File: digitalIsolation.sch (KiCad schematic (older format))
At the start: 9 parts, among them U14 74AHC1G14, U15 Si8651

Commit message: Extended board
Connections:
- net SDO: now also RP1.5 (R4); no longer R25.1
- net ~LDAC: now also R25.1; no longer RP1.5 (R4)
- net at U15.11 (B5): now also RP1.4 (P4); no longer R25.2
- net at U15.12 (B4): now also R25.2; no longer RP1.4 (P4)
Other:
- moved on the sheet: R25, RP1
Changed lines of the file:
@@
 Comment4 ""
 $EndDescr
-Text HLabel 8700 2250 2    60   Output ~ 0
+Text HLabel 8700 2200 2    60   Output ~ 0
 ~SS
-Text HLabel 8700 2350 2    60   Output ~ 0
+Text HLabel 8700 2300 2    60   Output ~ 0
 SCLK
-Text HLabel 8700 2450 2    60   Output ~ 0
+Text HLabel 8700 2400 2    60   Output ~ 0
 SDI
-Text HLabel 8700 2800 2    60   Input ~ 0
+Text HLabel 8700 2500 2    60   Input ~ 0
 SDO
-Text HLabel 8700 2550 2    60   Output ~ 0
+Text HLabel 8700 2700 2    60   Output ~ 0
 ~LDAC
 $Comp
@@
 $EndComp
 Wire Wire Line
-	8000 2350 7700 2350
-Wire Wire Line
-	7700 2800 8050 2800
-Wire Wire Line
 	7700 2950 7800 2950
 Wire Wire Line
@@
 	6400 3500 6300 3500
 Wire Wire Line
-	6300 3500 6300 3800
+	6300 3800 6300 3500
 $Comp
 L C C73
@@
 	4400 3650 4400 3800
 Wire Wire Line
-	6300 3800 3600 3800
+	3600 3800 6300 3800
 Connection ~ 5200 3800
 Connection ~ 6000 3800
@@
 L R R25
 U 1 1 56E0FC32
-P 8200 2800
-F 0 "R25" V 8280 2800 50  0000 C CNN
-F 1 "150" V 8200 2800 50  0000 C CNN
-F 2 "Resistors_SMD:R_0805" V 8130 2800 50  0001 C CNN
-F 3 "" H 8200 2800 50  0000 C CNN
-F 4 "MCWR08X1500FTL" H 8200 2800 60  0001 C CNN "Part Number"
-F 5 "Multicomp" H 8200 2800 60  0001 C CNN "Manufacturer"
-F 6 "0805" H 8200 2800 60  0001 C CNN "Package"
-F 7 "Farnell" H 8200 2800 60  0001 C CNN "Supplier"
-F 8 "2447574" H 8200 2800 60  0001 C CNN "Order Code"
-F 9 "Mouser" H 8200 2800 60  0001 C CNN "Alt. Supplier"
-F 10 "71-TNPW0805150RFEEA" H 8200 2800 60  0001 C CNN "Alt. Order Code"
-F 11 "150Ω/1% 0805 resistor" H 8200 2800 60  0001 C CNN "Note"
-	1    8200 2800
+P 8200 2700
+F 0 "R25" V 8280 2700 50  0000 C CNN
+F 1 "150" V 8200 2700 50  0000 C CNN
+F 2 "Resistors_SMD:R_0805" V 8130 2700 50  0001 C CNN
+F 3 "" H 8200 2700 50  0000 C CNN
+F 4 "MCWR08X1500FTL" H 8200 2700 60  0001 C CNN "Part Number"
+F 5 "Multicomp" H 8200 2700 60  0001 C CNN "Manufacturer"
+F 6 "0805" H 8200 2700 60  0001 C CNN "Package"
+F 7 "Farnell" H 8200 2700 60  0001 C CNN "Supplier"
+F 8 "2447574" H 8200 2700 60  0001 C CNN "Order Code"
+F 9 "Mouser" H 8200 2700 60  0001 C CNN "Alt. Supplier"
+F 10 "71-TNPW0805150RFEEA" H 8200 2700 60  0001 C CNN "Alt. Order Code"
+F 11 "150Ω/1% 0805 resistor" H 8200 2700 60  0001 C CNN "Note"
+	1    8200 2700
 	0    1    1    0
 $EndComp
 Wire Wire Line
-	8400 2250 8700 2250
-Wire Wire Line
-	8400 2350 8700 2350
-Wire Wire Line
-	8400 2450 8700 2450
-Wire Wire Line
-	8400 2550 8700 2550
-Wire Wire Line
-	8350 2800 8700 2800
+	8400 2200 8700 2200
+Wire Wire Line
+	8400 2300 8700 2300
+Wire Wire Line
+	8400 2400 8700 2400
+Wire Wire Line
+	8350 2700 8700 2700
+Wire Wire Line
+	8400 2500 8700 2500
 $Comp
 L R_PACK4 RP1
 U 1 1 56E10B8D
-P 8200 2600
-F 0 "RP1" H 8200 3050 50  0000 C CNN
-F 1 "4x150" H 8200 2550 50  0000 C CNN
-F 2 "Resistors_SMD:R_Array_Convex_4x0603" H 8200 2600 50  0001 C CNN
-F 3 "" H 8200 2600 50  0000 C CNN
-F 4 "YC164-JR-07150RL" H 8200 2600 60  0001 C CNN "Part Number"
-F 5 "Yageo" H 8200 2600 60  0001 C CNN "Manufacturer"
-F 6 "4×0603" H 8200 2600 60  0001 C CNN "Package"
-F 7 "Farnell" H 8200 2600 60  0001 C CNN "Supplier"
-F 8 "9234462" H 8200 2600 60  0001 C CNN "Order Code"
-F 9 "Mouser" H 8200 2600 60  0001 C CNN "Alt. Supplier"
-F 10 "603-YC164-JR-07150RL" H 8200 2600 60  0001 C CNN "Alt. Order Code"
-F 11 "4×150Ω/5% 0603 resistor array" H 8200 2600 60  0001 C CNN "Note"
-	1    8200 2600
-	1    0    0    -1
-$EndComp
-Wire Wire Line
-	7700 2200 7900 2200
-Wire Wire Line
-	7900 2200 7900 2250
-Wire Wire Line
-	7900 2250 8000 2250
-Wire Wire Line
-	8000 2450 7900 2450
-Wire Wire Line
-	7900 2450 7900 2500
-Wire Wire Line
-	7900 2500 7700 2500
-Wire Wire Line
-	7700 2650 7900 2650
-Wire Wire Line
-	7900 2650 7900 2550
-Wire Wire Line
-	7900 2550 8000 2550
+P 8200 2550
+F 0 "RP1" H 8200 3000 50  0000 C CNN
+F 1 "4x150" H 8200 2500 50  0000 C CNN
+F 2 "Resistors_SMD:R_Array_Convex_4x0603" H 8200 2550 50  0001 C CNN
+F 3 "" H 8200 2550 50  0000 C CNN
+F 4 "YC164-JR-07150RL" H 8200 2550 60  0001 C CNN "Part Number"
+F 5 "Yageo" H 8200 2550 60  0001 C CNN "Manufacturer"
+F 6 "4×0603" H 8200 2550 60  0001 C CNN "Package"
+F 7 "Farnell" H 8200 2550 60  0001 C CNN "Supplier"
+F 8 "9234462" H 8200 2550 60  0001 C CNN "Order Code"
+F 9 "Mouser" H 8200 2550 60  0001 C CNN "Alt. Supplier"
+F 10 "603-YC164-JR-07150RL" H 8200 2550 60  0001 C CNN "Alt. Order Code"
+F 11 "4×150Ω/5% 0603 resistor array" H 8200 2550 60  0001 C CNN "Note"
+	1    8200 2550
+	1    0    0    -1
+$EndComp
+Wire Wire Line
+	7700 2200 8000 2200
 $Comp
 L C C76
@@
 	1    0    0    -1
 $EndComp
+Wire Wire Line
+	8000 2300 7800 2300
+Wire Wire Line
+	7800 2300 7800 2350
+Wire Wire Line
+	7800 2350 7700 2350
+Wire Wire Line
+	8000 2400 7850 2400
+Wire Wire Line
+	7850 2400 7850 2500
+Wire Wire Line
+	7850 2500 7700 2500
+Wire Wire Line
+	8000 2500 7900 2500
+Wire Wire Line
+	7900 2500 7900 2800
+Wire Wire Line
+	7900 2800 7700 2800
+Wire Wire Line
+	7700 2650 7800 2650
+Wire Wire Line
+	7800 2650 7800 2700
+Wire Wire Line
+	7800 2700 8050 2700
 $EndSCHEMATC

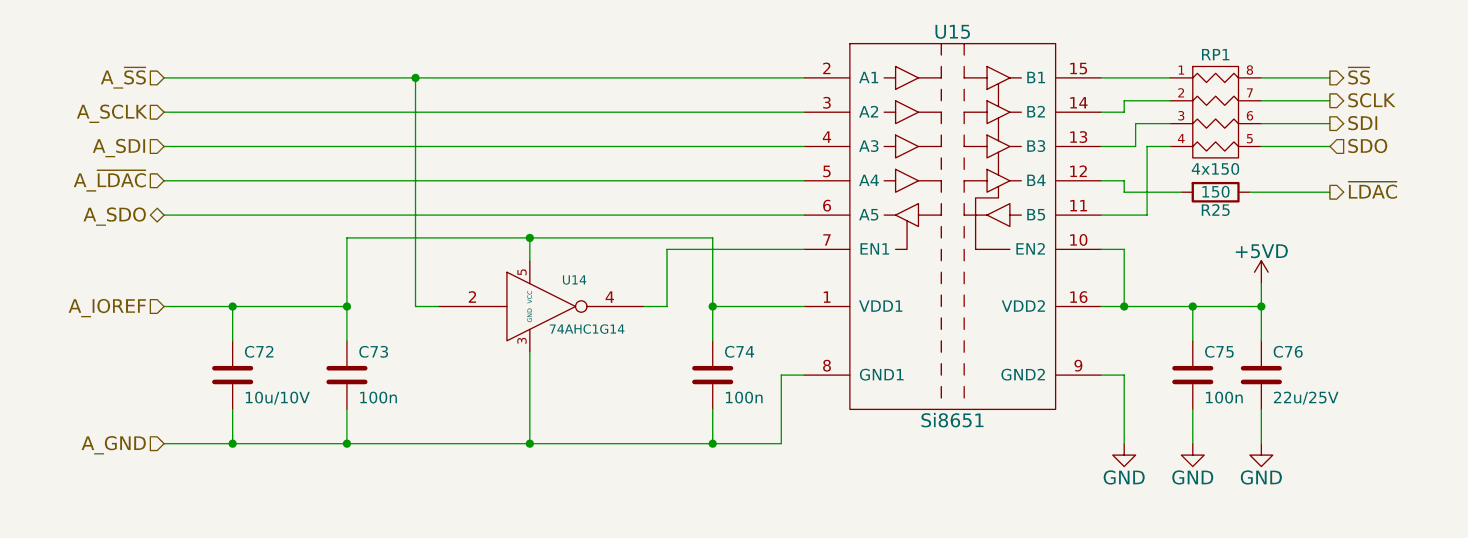
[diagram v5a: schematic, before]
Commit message: Fixed can, 1Ohm resistor descriptions
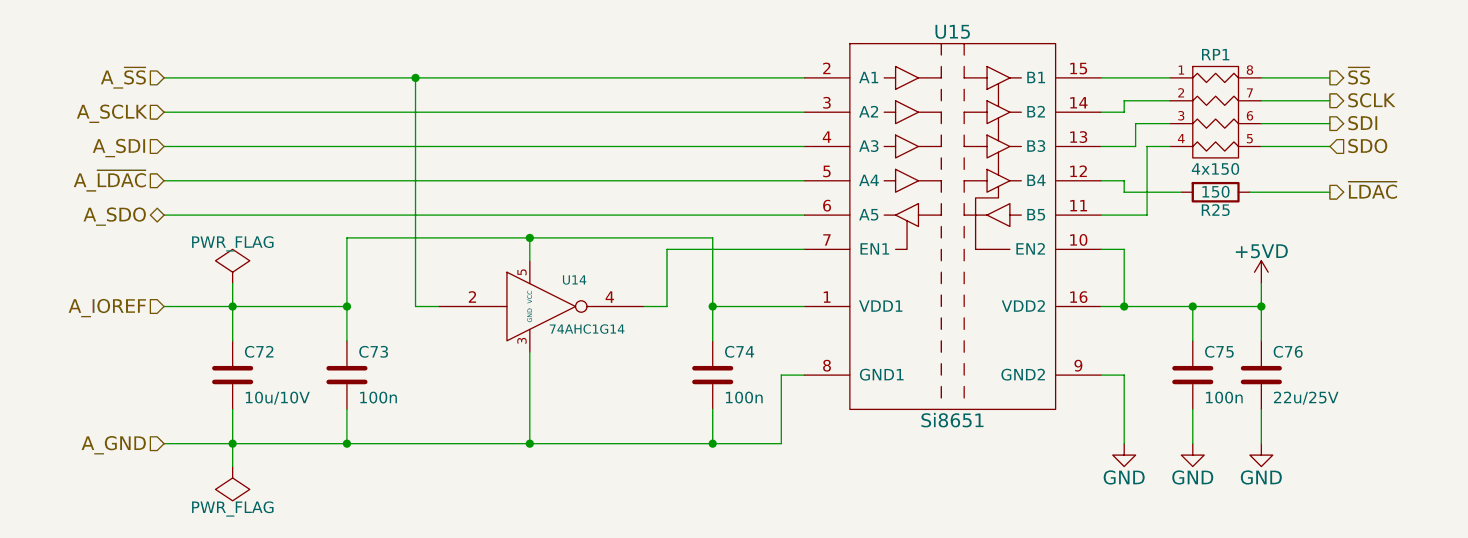
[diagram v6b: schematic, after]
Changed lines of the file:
@@
 	8100 3650 8100 3800
 $Comp
-L GND #PWR082
+L GND #PWR089
 U 1 1 5574AC81
 P 7800 3800
-F 0 "#PWR082" H 7800 3550 60  0001 C CNN
+F 0 "#PWR089" H 7800 3550 60  0001 C CNN
 F 1 "GND" H 7800 3650 60  0000 C CNN
 F 2 "" H 7800 3800 60  0000 C CNN
@@
 $EndComp
 $Comp
-L GND #PWR083
+L GND #PWR090
 U 1 1 5574ACAE
 P 8100 3800
-F 0 "#PWR083" H 8100 3550 60  0001 C CNN
+F 0 "#PWR090" H 8100 3550 60  0001 C CNN
 F 1 "GND" H 8100 3650 60  0000 C CNN
 F 2 "" H 8100 3800 60  0000 C CNN
@@
 	6400 3500 6300 3500
 Wire Wire Line
-	6300 3800 6300 3500
+	6300 3500 6300 3800
 $Comp
 L C C73
@@
 	4400 3650 4400 3800
 Wire Wire Line
-	3600 3800 6300 3800
+	6300 3800 3600 3800
 Connection ~ 5200 3800
 Connection ~ 6000 3800
@@
 $EndComp
 Wire Wire Line
-	3900 3350 3900 3200
+	3900 3100 3900 3350
 Connection ~ 3900 3200
 Wire Wire Line
-	3900 3650 3900 3800
+	3900 3650 3900 3900
 Connection ~ 3900 3800
 $Comp
@@
 Connection ~ 8400 3200
 $Comp
-L +5VD #PWR084
+L +5VD #PWR091
 U 1 1 5574AC36
 P 8400 3100
-F 0 "#PWR084" H 8400 2950 60  0001 C CNN
+F 0 "#PWR091" H 8400 2950 60  0001 C CNN
 F 1 "+5VD" H 8400 3240 60  0000 C CNN
 F 2 "" H 8400 3100 60  0000 C CNN
@@
 	8400 3650 8400 3800
 $Comp
-L GND #PWR085
+L GND #PWR092
 U 1 1 56E16784
 P 8400 3800
-F 0 "#PWR085" H 8400 3550 60  0001 C CNN
+F 0 "#PWR092" H 8400 3550 60  0001 C CNN
 F 1 "GND" H 8400 3650 60  0000 C CNN
 F 2 "" H 8400 3800 60  0000 C CNN
@@
 Wire Wire Line
 	7800 2700 8050 2700
+$Comp
+L PWR_FLAG #FLG093
+U 1 1 56F3D1DA
+P 3900 3100
+F 0 "#FLG093" H 3900 3195 50  0001 C CNN
+F 1 "PWR_FLAG" H 3900 3280 50  0000 C CNN
+F 2 "" H 3900 3100 50  0000 C CNN
+F 3 "" H 3900 3100 50  0000 C CNN
+	1    3900 3100
+	1    0    0    -1
+$EndComp
+$Comp
+L PWR_FLAG #FLG094
+U 1 1 56F3D24A
+P 3900 3900
+F 0 "#FLG094" H 3900 3995 50  0001 C CNN
+F 1 "PWR_FLAG" H 3900 4080 50  0000 C CNN
+F 2 "" H 3900 3900 50  0000 C CNN
+F 3 "" H 3900 3900 50  0000 C CNN
+	1    3900 3900
+	-1   0    0    1
+$EndComp
 $EndSCHEMATC

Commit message: Finalized PCB for production
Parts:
- C72: Alt. Order Code 81-GRM21BR61A106KE19 -> 603-CC805KKX5R8BB106
- C73, C74, C75: Alt. Order Code 710-885012206095 -> 603-CC603KRX7R9BB104; Manufacturer Multicomp -> Yageo; Note 100n/50V X7R 0603 ceramic capacitor -> 100nF/50V X7R 0603 ceramic capacitor; Order Code 1759122 -> 1362556; Part Number MC0603B104K500CT -> CC0603KRX7R9BB104
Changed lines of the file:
@@
 Wire Wire Line
 	7700 3200 8400 3200
-$Comp
-L C C75
-U 1 1 5574AB6E
-P 8100 3500
-F 0 "C75" H 8150 3600 50  0000 L CNN
-F 1 "100n" H 8150 3400 50  0000 L CNN
-F 2 "Capacitors_SMD:C_0603" H 8138 3350 30  0001 C CNN
-F 3 "" H 8100 3500 60  0000 C CNN
-F 4 "MC0603B104K500CT" H 5300 7000 60  0001 C CNN "Part Number"
-F 5 "Multicomp" H 5300 7000 60  0001 C CNN "Manufacturer"
-F 6 "0603" H 8100 3500 60  0001 C CNN "Package"
-F 7 "Farnell" H 8100 3500 60  0001 C CNN "Supplier"
-F 8 "1759122" H 5300 7000 60  0001 C CNN "Order Code"
-F 9 "Mouser" H 8100 3500 60  0001 C CNN "Alt. Supplier"
-F 10 "710-885012206095" H 8100 3500 60  0001 C CNN "Alt. Order Code"
-F 11 "100n/50V X7R 0603 ceramic capacitor" H 8100 3500 60  0001 C CNN "Note"
-	1    8100 3500
-	1    0    0    -1
-$EndComp
 Wire Wire Line
 	8100 3200 8100 3350
@@
 	8100 3650 8100 3800
 $Comp
-L GND #PWR089
+L GND #PWR85
 U 1 1 5574AC81
 P 7800 3800
-F 0 "#PWR089" H 7800 3550 60  0001 C CNN
+F 0 "#PWR85" H 7800 3550 60  0001 C CNN
 F 1 "GND" H 7800 3650 60  0000 C CNN
 F 2 "" H 7800 3800 60  0000 C CNN
@@
 $EndComp
 $Comp
-L GND #PWR090
+L GND #PWR86
 U 1 1 5574ACAE
 P 8100 3800
-F 0 "#PWR090" H 8100 3550 60  0001 C CNN
+F 0 "#PWR86" H 8100 3550 60  0001 C CNN
 F 1 "GND" H 8100 3650 60  0000 C CNN
 F 2 "" H 8100 3800 60  0000 C CNN
@@
 	1    0    0    -1
 $EndComp
-$Comp
-L C C74
-U 1 1 5574AE37
-P 6000 3500
-F 0 "C74" H 6050 3600 50  0000 L CNN
-F 1 "100n" H 6050 3400 50  0000 L CNN
-F 2 "Capacitors_SMD:C_0603" H 6038 3350 30  0001 C CNN
-F 3 "" H 6000 3500 60  0000 C CNN
-F 4 "MC0603B104K500CT" H 5300 7000 60  0001 C CNN "Part Number"
-F 5 "Multicomp" H 5300 7000 60  0001 C CNN "Manufacturer"
-F 6 "0603" H 6000 3500 60  0001 C CNN "Package"
-F 7 "Farnell" H 6000 3500 60  0001 C CNN "Supplier"
-F 8 "1759122" H 5300 7000 60  0001 C CNN "Order Code"
-F 9 "Mouser" H 6000 3500 60  0001 C CNN "Alt. Supplier"
-F 10 "710-885012206095" H 6000 3500 60  0001 C CNN "Alt. Order Code"
-F 11 "100n/50V X7R 0603 ceramic capacitor" H 6000 3500 60  0001 C CNN "Note"
-	1    6000 3500
-	1    0    0    -1
-$EndComp
 Wire Wire Line
 	6000 3200 6400 3200
@@
 Wire Wire Line
 	6300 3500 6300 3800
-$Comp
-L C C73
-U 1 1 5574AD7F
-P 4400 3500
-F 0 "C73" H 4450 3600 50  0000 L CNN
-F 1 "100n" H 4450 3400 50  0000 L CNN
-F 2 "Capacitors_SMD:C_0603" H 4438 3350 30  0001 C CNN
-F 3 "" H 4400 3500 60  0000 C CNN
-F 4 "MC0603B104K500CT" H 5400 7000 60  0001 C CNN "Part Number"
-F 5 "Multicomp" H 5400 7000 60  0001 C CNN "Manufacturer"
-F 6 "0603" H 4400 3500 60  0001 C CNN "Package"
-F 7 "Farnell" H 4400 3500 60  0001 C CNN "Supplier"
-F 8 "1759122" H 5400 7000 60  0001 C CNN "Order Code"
-F 9 "Mouser" H 4400 3500 60  0001 C CNN "Alt. Supplier"
-F 10 "710-885012206095" H 4400 3500 60  0001 C CNN "Alt. Order Code"
-F 11 "100n/50V X7R 0603 ceramic capacitor" H 4400 3500 60  0001 C CNN "Note"
-	1    4400 3500
-	1    0    0    -1
-$EndComp
 Wire Wire Line
 	4800 3200 4700 3200
@@
 F 8 "1828805" H 3900 3500 60  0001 C CNN "Order Code"
 F 9 "Mouser" H 3900 3500 60  0001 C CNN "Alt. Supplier"
-F 10 "81-GRM21BR61A106KE19" H 3900 3500 60  0001 C CNN "Alt. Order Code"
+F 10 "603-CC805KKX5R8BB106" H 3900 3500 60  0001 C CNN "Alt. Order Code"
 F 11 "10μ/10V X5R 0805 ceramic capacitor" H 3900 3500 60  0001 C CNN "Note"
 	1    3900 3500
@@
 Connection ~ 8400 3200
 $Comp
-L +5VD #PWR091
+L +5VD #PWR87
 U 1 1 5574AC36
 P 8400 3100
-F 0 "#PWR091" H 8400 2950 60  0001 C CNN
+F 0 "#PWR87" H 8400 2950 60  0001 C CNN
 F 1 "+5VD" H 8400 3240 60  0000 C CNN
 F 2 "" H 8400 3100 60  0000 C CNN
@@
 	8400 3650 8400 3800
 $Comp
-L GND #PWR092
+L GND #PWR88
 U 1 1 56E16784
 P 8400 3800
-F 0 "#PWR092" H 8400 3550 60  0001 C CNN
+F 0 "#PWR88" H 8400 3550 60  0001 C CNN
 F 1 "GND" H 8400 3650 60  0000 C CNN
 F 2 "" H 8400 3800 60  0000 C CNN
@@
 	7800 2700 8050 2700
 $Comp
-L PWR_FLAG #FLG093
+L PWR_FLAG #FLG8
 U 1 1 56F3D1DA
 P 3900 3100
-F 0 "#FLG093" H 3900 3195 50  0001 C CNN
+F 0 "#FLG8" H 3900 3195 50  0001 C CNN
 F 1 "PWR_FLAG" H 3900 3280 50  0000 C CNN
 F 2 "" H 3900 3100 50  0000 C CNN
@@
 $EndComp
 $Comp
-L PWR_FLAG #FLG094
+L PWR_FLAG #FLG9
 U 1 1 56F3D24A
 P 3900 3900
-F 0 "#FLG094" H 3900 3995 50  0001 C CNN
+F 0 "#FLG9" H 3900 3995 50  0001 C CNN
 F 1 "PWR_FLAG" H 3900 4080 50  0000 C CNN
 F 2 "" H 3900 3900 50  0000 C CNN
@@
 	-1   0    0    1
 $EndComp
+$Comp
+L C C73
+U 1 1 56F34E94
+P 4400 3500
+F 0 "C73" H 4450 3600 50  0000 L CNN
+F 1 "100n" H 4450 3400 50  0000 L CNN
+F 2 "Capacitors_SMD:C_0603" H 4438 3350 30  0001 C CNN
+F 3 "" H 4400 3500 60  0000 C CNN
+F 4 "CC0603KRX7R9BB104" H 6150 8600 60  0001 C CNN "Part Number"
+F 5 "Yageo" H 6150 8600 60  0001 C CNN "Manufacturer"
+F 6 "0603" H 4400 3500 60  0001 C CNN "Package"
+F 7 "Farnell" H 4400 3500 60  0001 C CNN "Supplier"
+F 8 "1362556" H 6150 8600 60  0001 C CNN "Order Code"
+F 9 "Mouser" H 4400 3500 60  0001 C CNN "Alt. Supplier"
+F 10 "603-CC603KRX7R9BB104" H 4400 3500 60  0001 C CNN "Alt. Order Code"
+F 11 "100nF/50V X7R 0603 ceramic capacitor" H 4400 3500 60  0001 C CNN "Note"
+	1    4400 3500
+	1    0    0    -1
+$EndComp
+$Comp
+L C C74
+U 1 1 56F3500A
+P 6000 3500
+F 0 "C74" H 6050 3600 50  0000 L CNN
+F 1 "100n" H 6050 3400 50  0000 L CNN
+F 2 "Capacitors_SMD:C_0603" H 6038 3350 30  0001 C CNN
+F 3 "" H 6000 3500 60  0000 C CNN
+F 4 "CC0603KRX7R9BB104" H 7750 8600 60  0001 C CNN "Part Number"
+F 5 "Yageo" H 7750 8600 60  0001 C CNN "Manufacturer"
+F 6 "0603" H 6000 3500 60  0001 C CNN "Package"
+F 7 "Farnell" H 6000 3500 60  0001 C CNN "Supplier"
+F 8 "1362556" H 7750 8600 60  0001 C CNN "Order Code"
+F 9 "Mouser" H 6000 3500 60  0001 C CNN "Alt. Supplier"
+F 10 "603-CC603KRX7R9BB104" H 6000 3500 60  0001 C CNN "Alt. Order Code"
+F 11 "100nF/50V X7R 0603 ceramic capacitor" H 6000 3500 60  0001 C CNN "Note"
+	1    6000 3500
+	1    0    0    -1
+$EndComp
+$Comp
+L C C75
+U 1 1 56F35072
+P 8100 3500
+F 0 "C75" H 8150 3600 50  0000 L CNN
+F 1 "100n" H 8150 3400 50  0000 L CNN
+F 2 "Capacitors_SMD:C_0603" H 8138 3350 30  0001 C CNN
+F 3 "" H 8100 3500 60  0000 C CNN
+F 4 "CC0603KRX7R9BB104" H 9850 8600 60  0001 C CNN "Part Number"
+F 5 "Yageo" H 9850 8600 60  0001 C CNN "Manufacturer"
+F 6 "0603" H 8100 3500 60  0001 C CNN "Package"
+F 7 "Farnell" H 8100 3500 60  0001 C CNN "Supplier"
+F 8 "1362556" H 9850 8600 60  0001 C CNN "Order Code"
+F 9 "Mouser" H 8100 3500 60  0001 C CNN "Alt. Supplier"
+F 10 "603-CC603KRX7R9BB104" H 8100 3500 60  0001 C CNN "Alt. Order Code"
+F 11 "100nF/50V X7R 0603 ceramic capacitor" H 8100 3500 60  0001 C CNN "Note"
+	1    8100 3500
+	1    0    0    -1
+$EndComp
 $EndSCHEMATC
